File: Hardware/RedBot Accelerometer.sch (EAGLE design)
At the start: 17 parts, among them U1 MMA8452Q, U2 MIC5205-3.3V

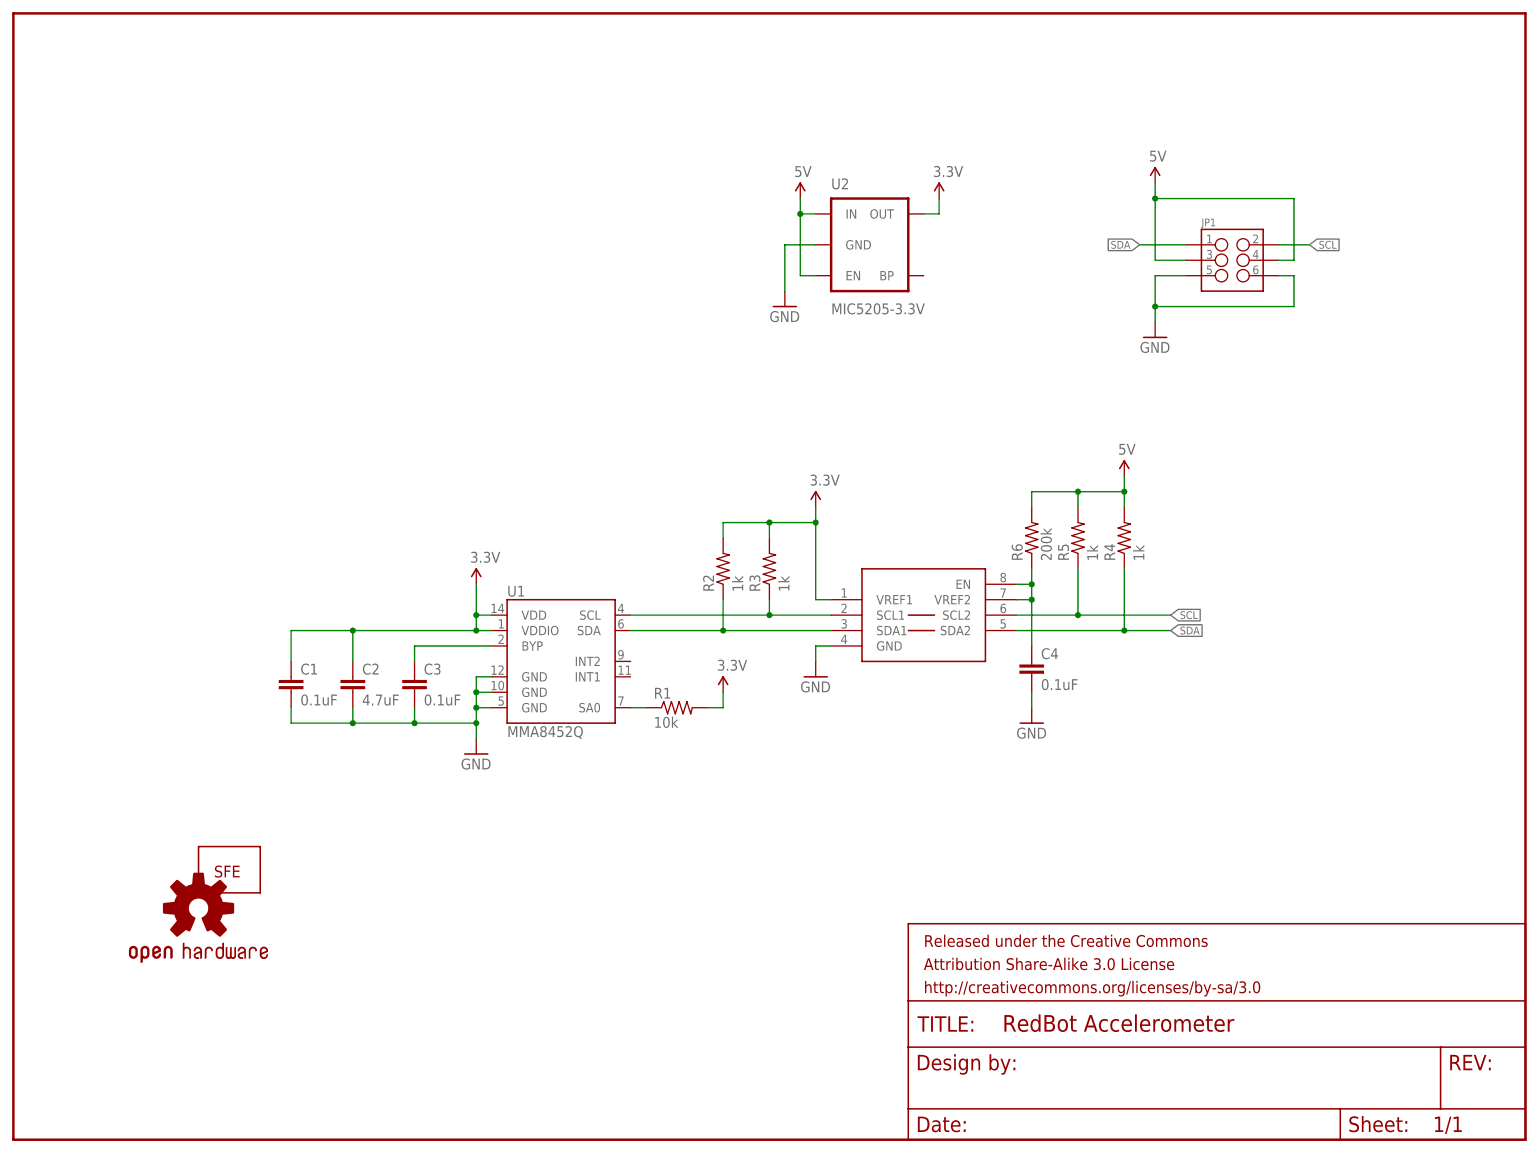
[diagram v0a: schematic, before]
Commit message: Add some part info for BOM purposes.
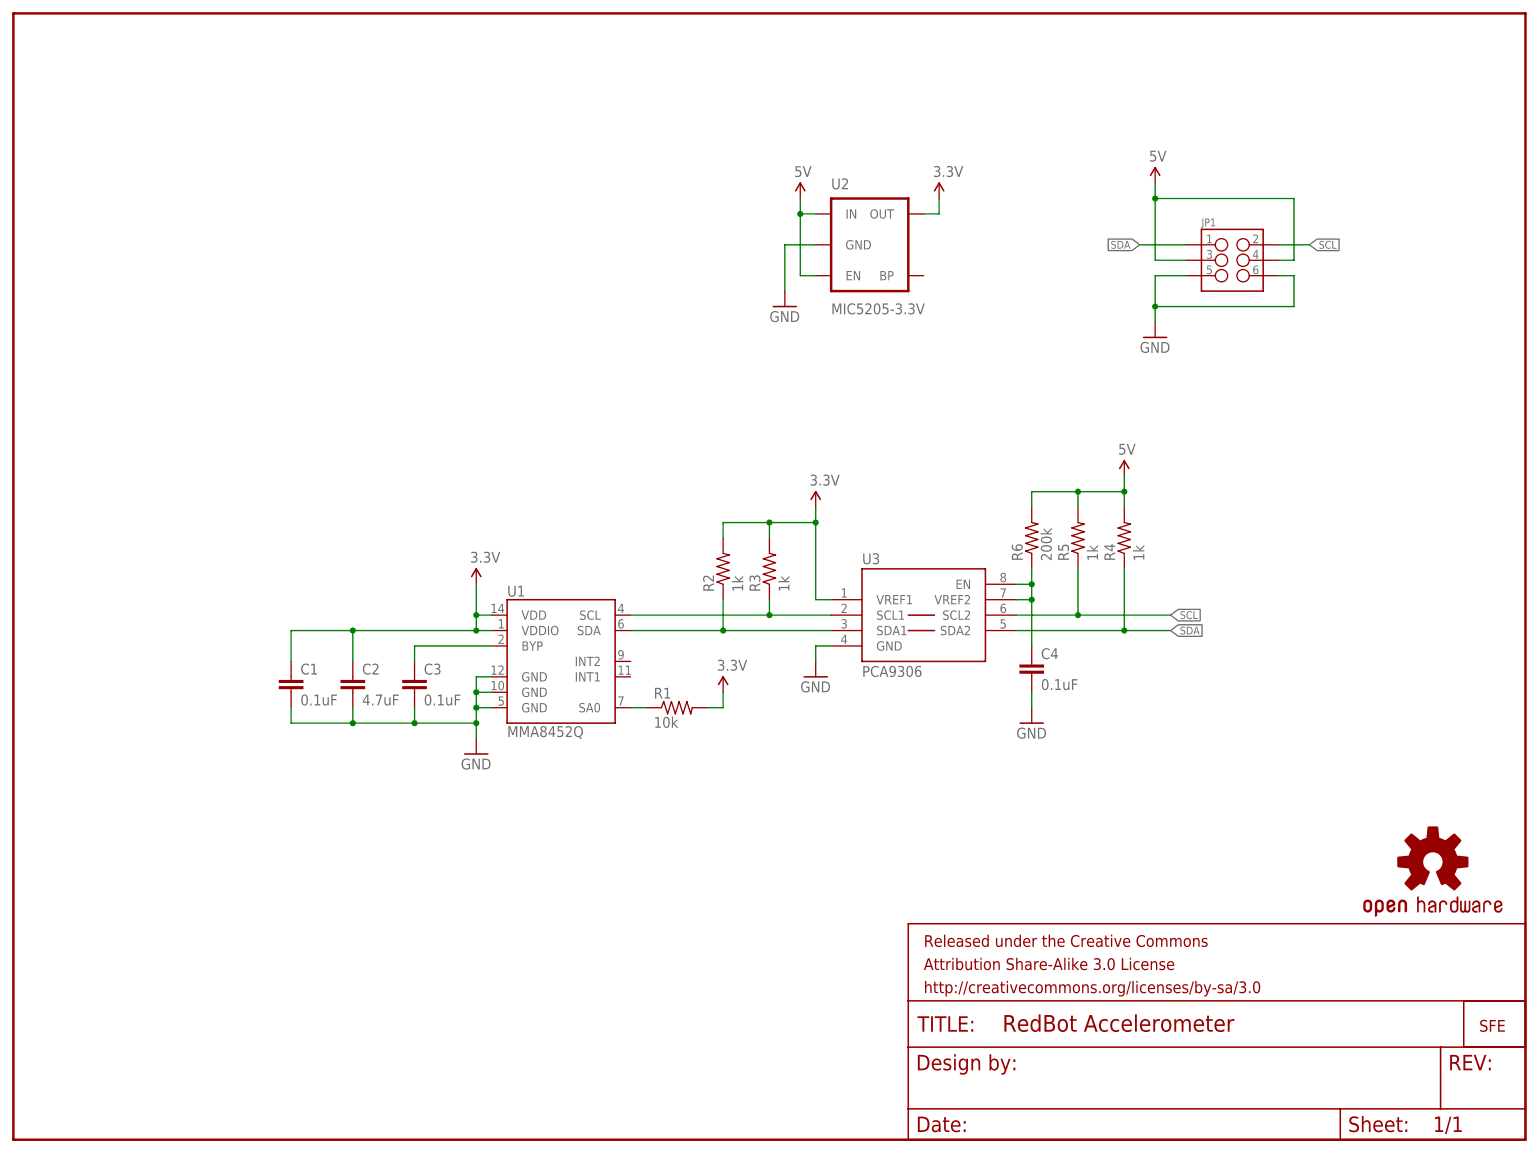
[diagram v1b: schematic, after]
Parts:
- renumbered U$1 to U3
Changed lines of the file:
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@@
 <part name="LOGO2" library="SparkFun-Aesthetics" deviceset="OSHW-LOGO" device="S"/>
 <part name="C1" library="SparkFun-Capacitors" deviceset="0.1UF-25V(+80/-20%)(0603)" device="" value="0.1uF"/>
-<part name="U$1" library="SparkFun-DigitalIC" deviceset="PCA9306" device=""/>
+<part name="U3" library="SparkFun-DigitalIC" deviceset="PCA9306" device="" value="PCA9306"/>
 <part name="U1" library="SparkFun-Sensors" deviceset="MMA8452Q" device=""/>
 <part name="R1" library="SparkFun-Resistors" deviceset="10KOHM1/10W1%(0603)" device="" value="10k"/>
@@
 <instance part="FRAME1" gate="G$1" x="0" y="0"/>
 <instance part="FRAME1" gate="G$2" x="147.32" y="0"/>
-<instance part="LOGO1" gate="G$1" x="33.02" y="43.18"/>
-<instance part="LOGO2" gate="G$1" x="30.48" y="38.1"/>
+<instance part="LOGO1" gate="G$1" x="241.3" y="17.78"/>
+<instance part="LOGO2" gate="G$1" x="233.68" y="45.72"/>
 <instance part="C1" gate="G$1" x="45.72" y="73.66"/>
-<instance part="U$1" gate="G$1" x="149.86" y="83.82"/>
+<instance part="U3" gate="G$1" x="149.86" y="83.82"/>
 <instance part="U1" gate="G$1" x="88.9" y="78.74"/>
 <instance part="R1" gate="G$1" x="109.22" y="71.12"/>
@@
 </segment>
 <segment>
-<pinref part="U$1" gate="G$1" pin="GND"/>
+<pinref part="U3" gate="G$1" pin="GND"/>
 <pinref part="GND3" gate="1" pin="GND"/>
 <wire x1="134.62" y1="81.28" x2="132.08" y2="81.28" width="0.1524" layer="91"/>
@@
 </segment>
 <segment>
-<pinref part="U$1" gate="G$1" pin="VREF1"/>
+<pinref part="U3" gate="G$1" pin="VREF1"/>
 <pinref part="SUPPLY5" gate="G$1" pin="3.3V"/>
 <wire x1="134.62" y1="88.9" x2="132.08" y2="88.9" width="0.1524" layer="91"/>
@@
 <net name="N$2" class="0">
 <segment>
-<pinref part="U$1" gate="G$1" pin="EN"/>
+<pinref part="U3" gate="G$1" pin="EN"/>
 <wire x1="165.1" y1="91.44" x2="167.64" y2="91.44" width="0.1524" layer="91"/>
 <pinref part="R6" gate="G$1" pin="1"/>
 <wire x1="167.64" y1="91.44" x2="167.64" y2="93.98" width="0.1524" layer="91"/>
-<pinref part="U$1" gate="G$1" pin="VREF2"/>
+<pinref part="U3" gate="G$1" pin="VREF2"/>
 <wire x1="165.1" y1="88.9" x2="167.64" y2="88.9" width="0.1524" layer="91"/>
 <wire x1="167.64" y1="88.9" x2="167.64" y2="91.44" width="0.1524" layer="91"/>
@@
 <net name="SCL" class="0">
 <segment>
-<pinref part="U$1" gate="G$1" pin="SCL2"/>
+<pinref part="U3" gate="G$1" pin="SCL2"/>
 <pinref part="R5" gate="G$1" pin="1"/>
 <wire x1="165.1" y1="86.36" x2="175.26" y2="86.36" width="0.1524" layer="91"/>
@@
 <net name="SDA" class="0">
 <segment>
-<pinref part="U$1" gate="G$1" pin="SDA2"/>
+<pinref part="U3" gate="G$1" pin="SDA2"/>
 <pinref part="R4" gate="G$1" pin="1"/>
 <wire x1="165.1" y1="83.82" x2="182.88" y2="83.82" width="0.1524" layer="91"/>
@@
 <net name="SCL1" class="0">
 <segment>
-<pinref part="U$1" gate="G$1" pin="SCL1"/>
+<pinref part="U3" gate="G$1" pin="SCL1"/>
 <pinref part="R3" gate="G$1" pin="1"/>
 <wire x1="134.62" y1="86.36" x2="124.46" y2="86.36" width="0.1524" layer="91"/>
@@
 <net name="SDA1" class="0">
 <segment>
-<pinref part="U$1" gate="G$1" pin="SDA1"/>
+<pinref part="U3" gate="G$1" pin="SDA1"/>
 <pinref part="R2" gate="G$1" pin="1"/>
 <wire x1="134.62" y1="83.82" x2="116.84" y2="83.82" width="0.1524" layer="91"/>

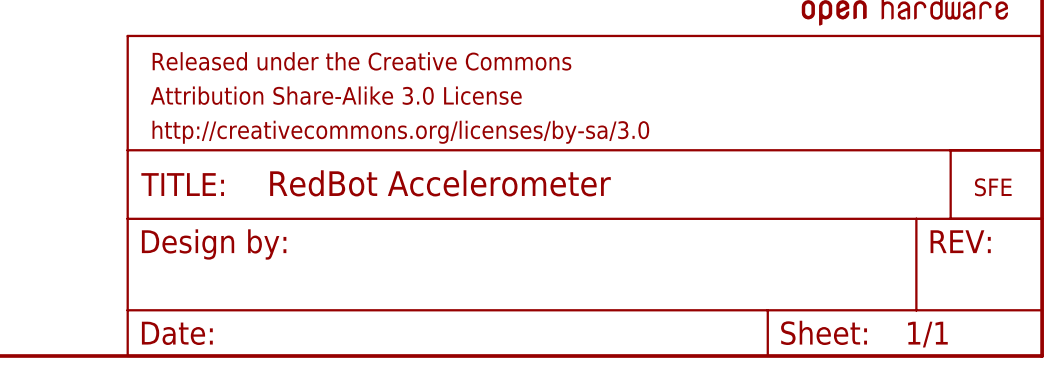
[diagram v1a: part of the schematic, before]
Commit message: Advance to rev 10 for release  - added pin numbers for alignment to top silk  - change revision numbers
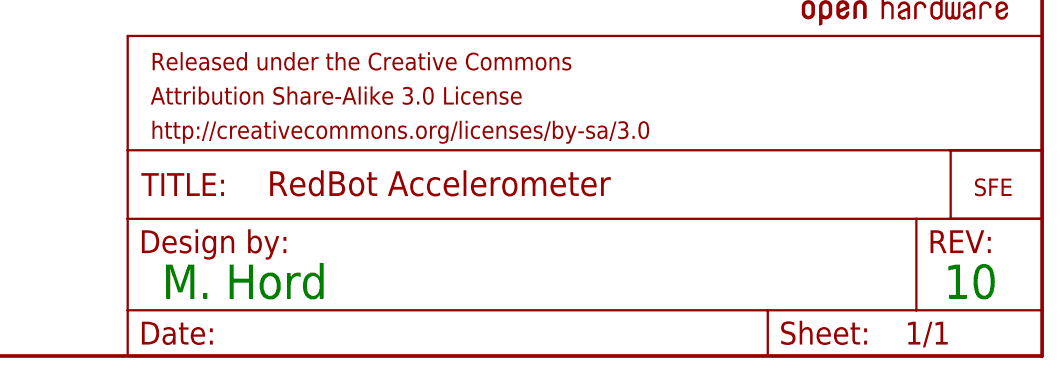
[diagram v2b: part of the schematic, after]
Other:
- note added: "10"
- note added: "M. Hord"
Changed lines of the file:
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@@
 <sheet>
 <plain>
+<text x="237.998" y="6.35" size="3.81" layer="91">10</text>
+<text x="151.13" y="6.35" size="3.81" layer="91">M. Hord</text>
 </plain>
 <instances>

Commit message: Rev for v11 protos
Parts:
- added JP2: (no value), SparkFun-Connectors:M03X2FEMALE_SMD
- C2: device SparkFun-Capacitors:4.7UF-6.3V-10%(0603) -> SparkFun-Capacitors:4.7UF-6.3V-10%(0603)0603
- JP1: device SparkFun-Connectors:M03X2NO_SILK -> SparkFun-Connectors:M03X2SMT
- R1: device SparkFun-Resistors:10KOHM1/10W1%(0603) -> SparkFun-Resistors:10KOHM1/10W1%(0603)0603
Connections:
- net 5V: now also JP2.3, JP2.4
- net GND: now also JP2.5, JP2.6
- net SCL: now also JP2.1
- net SDA: now also JP2.2
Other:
- note added: "Bottom side connector- Female"
- note added: "Top side connector- Male"
- moved on the sheet: JP1
